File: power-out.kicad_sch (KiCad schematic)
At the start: 1 part, among them U2 TPS61022

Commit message: Configure power output
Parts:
- added C2: 10µF, symbol Device:C
- added C3, C4: 22µF, symbol Device:C
- added JP1: SolderJumper_2_Open, Jumper:SolderJumper-3_P1.3mm_Open_RoundedPad1.0x1.5mm_NumberLabels, symbol Jumper:SolderJumper_3_Open
- added L1: 1µH, symbol Device:L
- added R3: 402kΩ 1% 125mW, Resistor_SMD:R_0805_2012Metric_Pad1.20x1.40mm_HandSolder, symbol Device:R
- added R4: 88.7kΩ 1% 125mW, Resistor_SMD:R_0805_2012Metric_Pad1.20x1.40mm_HandSolder, symbol Device:R
- added R5, R6: 10kΩ 125mW, Resistor_SMD:R_0805_2012Metric_Pad1.20x1.40mm_HandSolder, symbol Device:R
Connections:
- net GND: now also C2.2, C3.2, C4.2, R4.2, R6.2
- net SUPERCAP: now also U2.5 (EN), C2.1, L1.1, R5.1
- net VOUT: now also C3.1, C4.1, R3.1
- net at U2.2 (SW): now also L1.2
- net at U2.4 (FB): now also R3.2, R4.1
- net at U2.6 (MODE): now also JP1.2 (C)
- new net: JP1.3 (B), R5.2
- new net: JP1.1 (A), R6.1
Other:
- moved on the sheet: U2

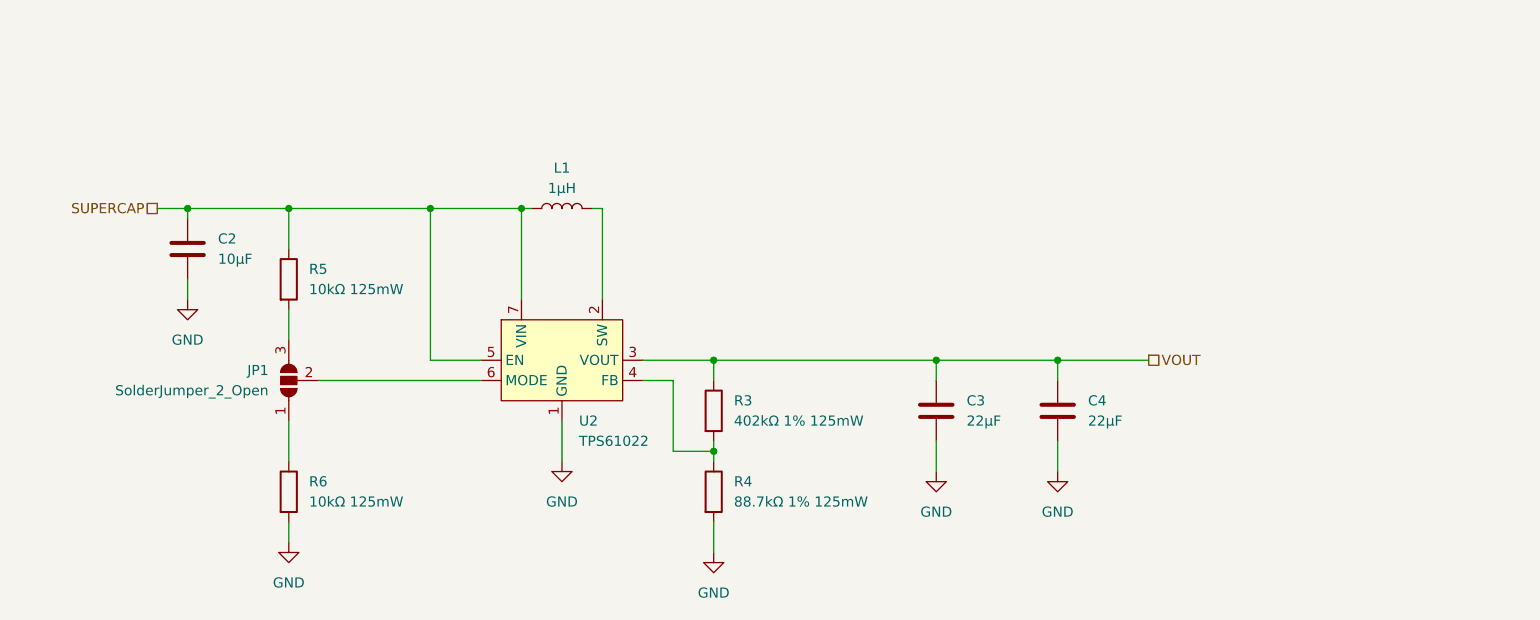
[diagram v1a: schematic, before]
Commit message: Add power output capacitors
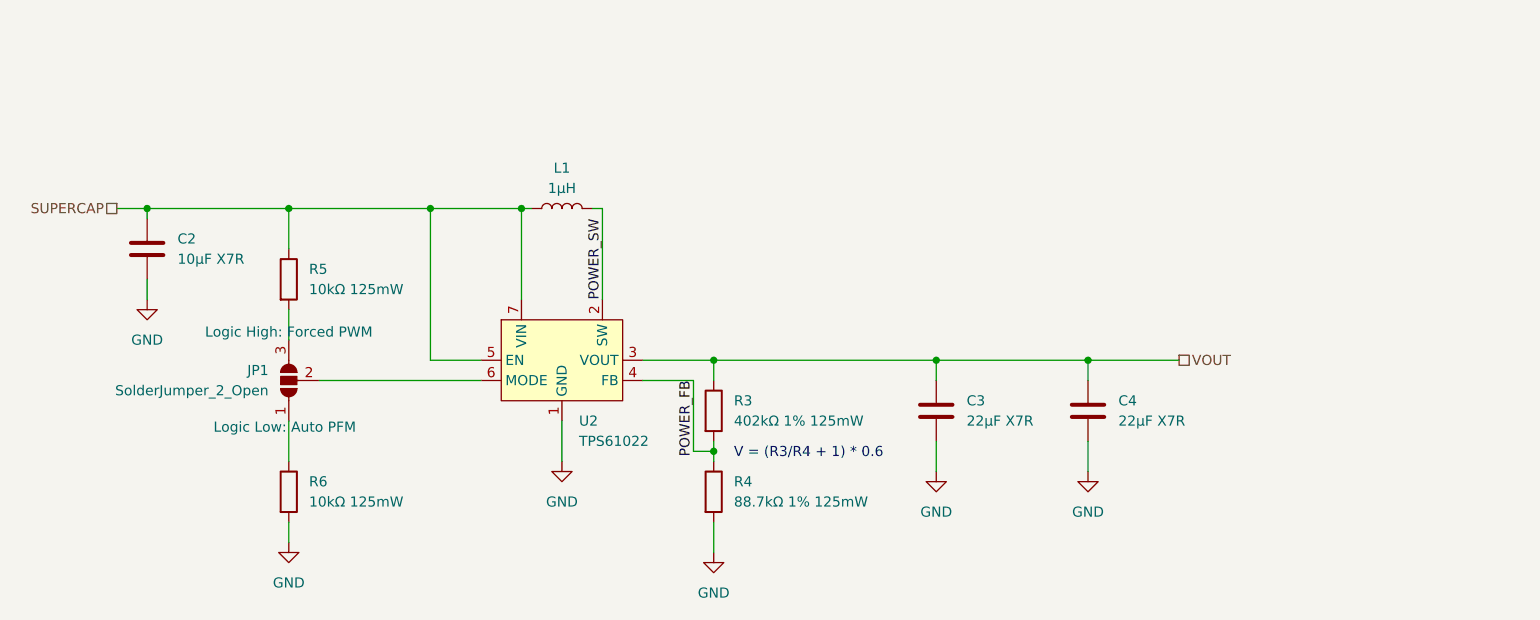
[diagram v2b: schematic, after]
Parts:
- C2: value 10µF -> 10µF X7R; footprint (none) -> Capacitor_SMD:C_0805_2012Metric_Pad1.18x1.45mm_HandSolder
- C3, C4: value 22µF -> 22µF X7R; footprint (none) -> Capacitor_SMD:C_0805_2012Metric_Pad1.18x1.45mm_HandSolder
- JP1: Logic High (none) -> Forced PWM; Logic Low (none) -> Auto PFM
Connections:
- net POWER_FB: now reaches R3.2, R4.1, U2.4 (FB)
- net POWER_SW: now reaches L1.2, U2.2 (SW)
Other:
- note added: "V = (R3/R4 + 1) * 0.6"
- moved on the sheet: C2, C4
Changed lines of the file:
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@@
 	(generator_version "9.0")
 	(paper "A4")
+	(text "V = (R3/R4 + 1) * 0.6"
+		(exclude_from_sim no)
+		(at 92.71 61.214 0)
+		(effects
+			(font
+				(size 1.27 1.27)
+			)
+			(justify left)
+		)
+	)
 	(junction
 		(at 90.17 49.53)
@@
 	)
 	(junction
-		(at 24.13 30.48)
+		(at 19.05 30.48)
 		(diameter 0)
 		(color 0 0 0 0)
@@
 	)
 	(junction
-		(at 133.35 49.53)
+		(at 137.16 49.53)
 		(diameter 0)
 		(color 0 0 0 0)
@@
 	(wire
 		(pts
+			(xy 118.11 49.53) (xy 137.16 49.53)
+		)
+		(stroke
+			(width 0)
+			(type default)
+		)
+	)
+	(wire
+		(pts
 			(xy 36.83 46.99) (xy 36.83 43.18)
 		)
@@
 	(wire
 		(pts
-			(xy 85.09 60.96) (xy 90.17 60.96)
-		)
-		(stroke
-			(width 0)
-			(type default)
-		)
-	)
-	(wire
-		(pts
-			(xy 133.35 49.53) (xy 144.78 49.53)
+			(xy 87.63 60.96) (xy 90.17 60.96)
+		)
+		(stroke
+			(width 0)
+			(type default)
+		)
+	)
+	(wire
+		(pts
+			(xy 137.16 49.53) (xy 148.59 49.53)
 		)
 		(stroke
@@
 	(wire
 		(pts
-			(xy 24.13 39.37) (xy 24.13 41.91)
+			(xy 19.05 39.37) (xy 19.05 41.91)
 		)
 		(stroke
@@
 	(wire
 		(pts
-			(xy 118.11 49.53) (xy 133.35 49.53)
-		)
-		(stroke
-			(width 0)
-			(type default)
-		)
-	)
-	(wire
-		(pts
-			(xy 24.13 31.75) (xy 24.13 30.48)
-		)
-		(stroke
-			(width 0)
-			(type default)
-		)
-	)
-	(wire
-		(pts
-			(xy 133.35 49.53) (xy 133.35 52.07)
-		)
-		(stroke
-			(width 0)
-			(type default)
-		)
-	)
-	(wire
-		(pts
-			(xy 85.09 52.07) (xy 85.09 60.96)
-		)
-		(stroke
-			(width 0)
-			(type default)
-		)
-	)
-	(wire
-		(pts
-			(xy 24.13 30.48) (xy 36.83 30.48)
+			(xy 19.05 31.75) (xy 19.05 30.48)
+		)
+		(stroke
+			(width 0)
+			(type default)
+		)
+	)
+	(wire
+		(pts
+			(xy 137.16 49.53) (xy 137.16 52.07)
+		)
+		(stroke
+			(width 0)
+			(type default)
+		)
+	)
+	(wire
+		(pts
+			(xy 87.63 52.07) (xy 87.63 60.96)
+		)
+		(stroke
+			(width 0)
+			(type default)
+		)
+	)
+	(wire
+		(pts
+			(xy 19.05 30.48) (xy 36.83 30.48)
 		)
 		(stroke
@@
 	(wire
 		(pts
-			(xy 133.35 59.69) (xy 133.35 63.5)
+			(xy 137.16 59.69) (xy 137.16 63.5)
 		)
 		(stroke
@@
 	(wire
 		(pts
-			(xy 81.28 52.07) (xy 85.09 52.07)
+			(xy 81.28 52.07) (xy 87.63 52.07)
 		)
 		(stroke
@@
 	(wire
 		(pts
-			(xy 20.32 30.48) (xy 24.13 30.48)
+			(xy 15.24 30.48) (xy 19.05 30.48)
 		)
 		(stroke
@@
 		)
 	)
-	(hierarchical_label "VOUT"
-		(shape passive)
-		(at 144.78 49.53 0)
+	(label "POWER_SW"
+		(at 76.2 31.75 270)
 		(effects
 			(font
 				(size 1.27 1.27)
 			)
-			(justify left)
-		)
-	)
-	(hierarchical_label "SUPERCAP"
-		(shape passive)
-		(at 20.32 30.48 180)
+			(justify right bottom)
+		)
+	)
+	(label "POWER_FB"
+		(at 87.63 52.07 270)
 		(effects
 			(font
 				(size 1.27 1.27)
 			)
+			(justify right bottom)
+		)
+	)
+	(hierarchical_label "VOUT"
+		(shape passive)
+		(at 148.59 49.53 0)
+		(effects
+			(font
+				(size 1.27 1.27)
+			)
+			(justify left)
+		)
+	)
+	(hierarchical_label "SUPERCAP"
+		(shape passive)
+		(at 15.24 30.48 180)
+		(effects
+			(font
+				(size 1.27 1.27)
+			)
 			(justify right)
 		)
@@
 	(symbol
 		(lib_id "Device:C")
-		(at 24.13 35.56 0)
+		(at 19.05 35.56 0)
 		(unit 1)
 		(exclude_from_sim no)
@@
 		(fields_autoplaced yes)
 		(property "Reference" "C2"
-			(at 27.94 34.2899 0)
-			(effects
-				(font
-					(size 1.27 1.27)
-				)
-				(justify left)
-			)
-		)
-		(property "Value" "10µF"
-			(at 27.94 36.8299 0)
-			(effects
-				(font
-					(size 1.27 1.27)
-				)
-				(justify left)
-			)
-		)
-		(property "Footprint" ""
-			(at 25.0952 39.37 0)
+			(at 22.86 34.2899 0)
+			(effects
+				(font
+					(size 1.27 1.27)
+				)
+				(justify left)
+			)
+		)
+		(property "Value" "10µF X7R"
+			(at 22.86 36.8299 0)
+			(effects
+				(font
+					(size 1.27 1.27)
+				)
+				(justify left)
+			)
+		)
+		(property "Footprint" "Capacitor_SMD:C_0805_2012Metric_Pad1.18x1.45mm_HandSolder"
+			(at 20.0152 39.37 0)
 			(effects
 				(font
@@
 		)
 		(property "Datasheet" "~"
-			(at 24.13 35.56 0)
+			(at 19.05 35.56 0)
 			(effects
 				(font
@@
 		)
 		(property "Description" "Unpolarized capacitor"
-			(at 24.13 35.56 0)
+			(at 19.05 35.56 0)
 			(effects
 				(font
@@
 	(symbol
 		(lib_id "Device:C")
-		(at 133.35 55.88 0)
+		(at 137.16 55.88 0)
 		(unit 1)
 		(exclude_from_sim no)
@@
 		(fields_autoplaced yes)
 		(property "Reference" "C4"
-			(at 137.16 54.6099 0)
-			(effects
-				(font
-					(size 1.27 1.27)
-				)
-				(justify left)
-			)
-		)
-		(property "Value" "22µF"
-			(at 137.16 57.1499 0)
-			(effects
-				(font
-					(size 1.27 1.27)
-				)
-				(justify left)
-			)
-		)
-		(property "Footprint" ""
-			(at 134.3152 59.69 0)
+			(at 140.97 54.6099 0)
+			(effects
+				(font
+					(size 1.27 1.27)
+				)
+				(justify left)
+			)
+		)
+		(property "Value" "22µF X7R"
+			(at 140.97 57.1499 0)
+			(effects
+				(font
+					(size 1.27 1.27)
+				)
+				(justify left)
+			)
+		)
+		(property "Footprint" "Capacitor_SMD:C_0805_2012Metric_Pad1.18x1.45mm_HandSolder"
+			(at 138.1252 59.69 0)
 			(effects
 				(font
@@
 		)
 		(property "Datasheet" "~"
-			(at 133.35 55.88 0)
+			(at 137.16 55.88 0)
 			(effects
 				(font
@@
 		)
 		(property "Description" "Unpolarized capacitor"
-			(at 133.35 55.88 0)
+			(at 137.16 55.88 0)
 			(effects
 				(font
@@
 	(symbol
 		(lib_id "power:GND")
-		(at 24.13 41.91 0)
+		(at 19.05 41.91 0)
 		(unit 1)
 		(exclude_from_sim no)
@@
 		(fields_autoplaced yes)
 		(property "Reference" "#PWR010"
-			(at 24.13 48.26 0)
+			(at 19.05 48.26 0)
 			(effects
 				(font
@@
 		)
 		(property "Value" "GND"
-			(at 24.13 46.99 0)
+			(at 19.05 46.99 0)
 			(effects
 				(font
@@
 		)
 		(property "Footprint" ""
-			(at 24.13 41.91 0)
+			(at 19.05 41.91 0)
 			(effects
 				(font
@@
 		)
 		(property "Datasheet" ""
-			(at 24.13 41.91 0)
+			(at 19.05 41.91 0)
 			(effects
 				(font
@@
 		)
 		(property "Description" "Power symbol creates a global label with name \"GND\" , ground"
-			(at 24.13 41.91 0)
+			(at 19.05 41.91 0)
 			(effects
 				(font
@@
 			)
 		)
-		(property "Value" "22µF"
+		(property "Value" "22µF X7R"
 			(at 121.92 57.1499 0)
 			(effects
@@
 			)
 		)
-		(property "Footprint" ""
+		(property "Footprint" "Capacitor_SMD:C_0805_2012Metric_Pad1.18x1.45mm_HandSolder"
 			(at 119.0752 59.69 0)
 			(effects
@@
 	(symbol
 		(lib_id "power:GND")
-		(at 133.35 63.5 0)
+		(at 137.16 63.5 0)
 		(unit 1)
 		(exclude_from_sim no)
@@
 		(fields_autoplaced yes)
 		(property "Reference" "#PWR011"
-			(at 133.35 69.85 0)
+			(at 137.16 69.85 0)
 			(effects
 				(font
@@
 		)
 		(property "Value" "GND"
-			(at 133.35 68.58 0)
+			(at 137.16 68.58 0)
 			(effects
 				(font
@@
 		)
 		(property "Footprint" ""
-			(at 133.35 63.5 0)
+			(at 137.16 63.5 0)
 			(effects
 				(font
@@
 		)
 		(property "Datasheet" ""
-			(at 133.35 63.5 0)
+			(at 137.16 63.5 0)
 			(effects
 				(font
@@
 		)
 		(property "Description" "Power symbol creates a global label with name \"GND\" , ground"
-			(at 133.35 63.5 0)
+			(at 137.16 63.5 0)
 			(effects
 				(font
@@
 		(on_board yes)
 		(dnp no)
-		(fields_autoplaced yes)
 		(property "Reference" "JP1"
 			(at 34.29 50.7999 90)
@@
 			)
 		)
+		(property "Logic High" "Forced PWM"
+			(at 36.83 45.974 90)
+			(show_name yes)
+			(effects
+				(font
+					(size 1.27 1.27)
+				)
+			)
+		)
+		(property "Logic Low" "Auto PFM"
+			(at 36.322 57.912 90)
+			(show_name yes)
+			(effects
+				(font
+					(size 1.27 1.27)
+				)
+			)
+		)

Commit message: Add inductor and finish power out layout
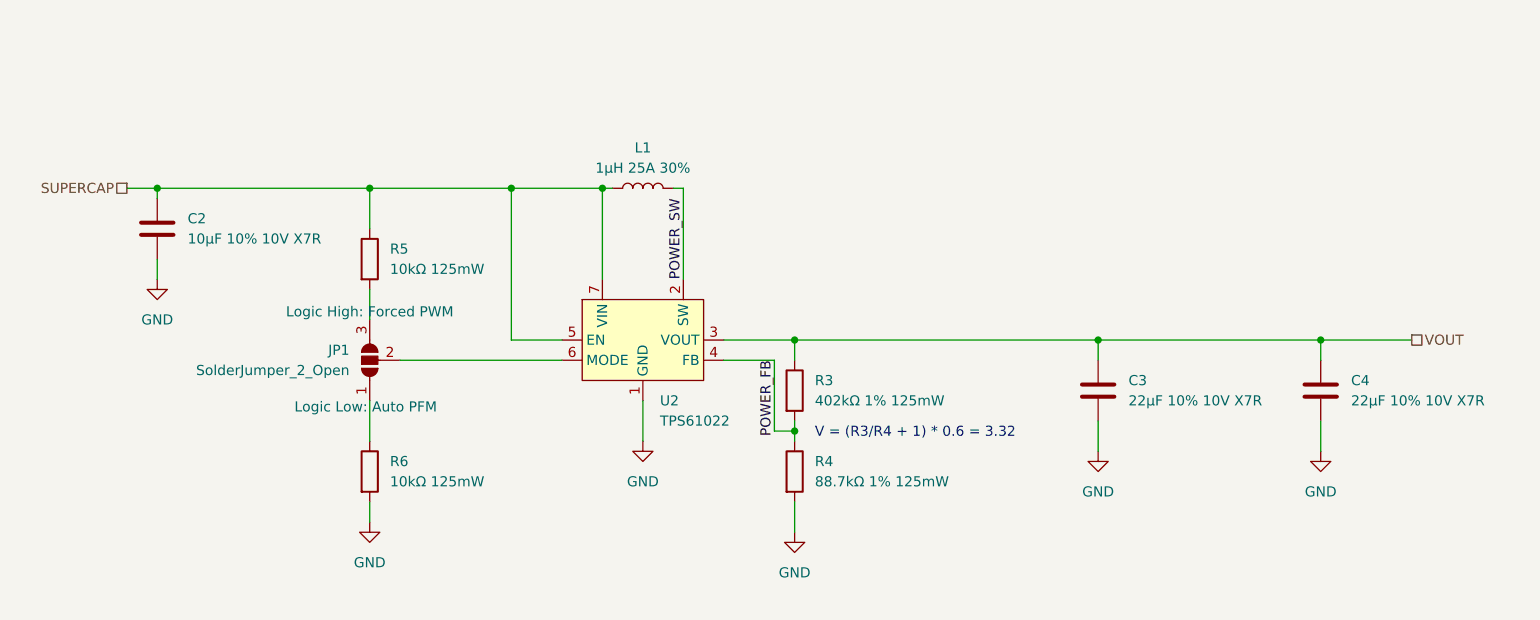
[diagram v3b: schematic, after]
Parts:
- C2: value 10µF X7R -> 10µF 10% 10V X7R
- C3, C4: value 22µF X7R -> 22µF 10% 10V X7R; footprint Capacitor_SMD:C_0805_2012Metric_Pad1.18x1.45mm_HandSolder -> Capacitor_SMD:C_1206_3216Metric_Pad1.33x1.80mm_HandSolder
- L1: value 1µH -> 1µH 25A 30%; footprint (none) -> Inductor_SMD:L_Bourns_SRP1245A
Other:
- note added: "V = (R3/R4 + 1) * 0.6 = 3.32"
- note removed: "V = (R3/R4 + 1) * 0.6"
- moved on the sheet: C2, C3, C4, JP1, L1, R3, R4, R5, R6, U2

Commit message: Prefix all of the references so that the numbering is manageable across multiple circuits
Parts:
- renumbered C2 to P.C1, C3 to P.C2, C4 to P.C3, JP1 to P.JP1, L1 to P.L1, R3 to P.R1, R4 to P.R2, R5 to P.R3, R6 to P.R4, U2 to P.U1
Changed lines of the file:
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@@
 		(dnp no)
 		(fields_autoplaced yes)
-		(property "Reference" "C2"
+		(property "Reference" "P.C1"
 			(at 24.13 31.7499 0)
 			(effects
@@
 			(project ""
 				(path "/01e6e533-9ed1-4dde-bac5-1959ff8991e5/08e0040f-7161-45a0-9f3d-7aa124b5aeed"
-					(reference "C2")
+					(reference "P.C1")
 					(unit 1)
 				)
@@
 		(dnp no)
 		(fields_autoplaced yes)
-		(property "Reference" "R4"
+		(property "Reference" "P.R2"
 			(at 102.87 62.2299 0)
 			(effects
@@
 			(project ""
 				(path "/01e6e533-9ed1-4dde-bac5-1959ff8991e5/08e0040f-7161-45a0-9f3d-7aa124b5aeed"
-					(reference "R4")
+					(reference "P.R2")
 					(unit 1)
 				)
@@
 		(dnp no)
 		(fields_autoplaced yes)
-		(property "Reference" "L1"
+		(property "Reference" "P.L1"
 			(at 81.28 22.86 90)
 			(effects
@@
 			(project ""
 				(path "/01e6e533-9ed1-4dde-bac5-1959ff8991e5/08e0040f-7161-45a0-9f3d-7aa124b5aeed"
-					(reference "L1")
+					(reference "P.L1")
 					(unit 1)
 				)
@@
 		(dnp no)
 		(fields_autoplaced yes)
-		(property "Reference" "C4"
+		(property "Reference" "P.C3"
 			(at 170.18 52.0699 0)
 			(effects
@@
 			(project "wireless-3v3-supercap"
 				(path "/01e6e533-9ed1-4dde-bac5-1959ff8991e5/08e0040f-7161-45a0-9f3d-7aa124b5aeed"
-					(reference "C4")
+					(reference "P.C3")
 					(unit 1)
 				)
@@
 		(dnp no)
 		(fields_autoplaced yes)
-		(property "Reference" "C3"
+		(property "Reference" "P.C2"
 			(at 142.24 52.0699 0)
 			(effects
@@
 			(project ""
 				(path "/01e6e533-9ed1-4dde-bac5-1959ff8991e5/08e0040f-7161-45a0-9f3d-7aa124b5aeed"
-					(reference "C3")
+					(reference "P.C2")
 					(unit 1)
 				)
@@
 		(dnp no)
 		(fields_autoplaced yes)
-		(property "Reference" "R5"
+		(property "Reference" "P.R3"
 			(at 49.53 35.5599 0)
 			(effects
@@
 			(project ""
 				(path "/01e6e533-9ed1-4dde-bac5-1959ff8991e5/08e0040f-7161-45a0-9f3d-7aa124b5aeed"
-					(reference "R5")
+					(reference "P.R3")
 					(unit 1)
 				)
@@
 		(dnp no)
 		(fields_autoplaced yes)
-		(property "Reference" "R3"
+		(property "Reference" "P.R1"
 			(at 102.87 52.0699 0)
 			(effects
@@
 			(project ""
 				(path "/01e6e533-9ed1-4dde-bac5-1959ff8991e5/08e0040f-7161-45a0-9f3d-7aa124b5aeed"
-					(reference "R3")
+					(reference "P.R1")
 					(unit 1)
 				)
@@
 		(dnp no)
 		(fields_autoplaced yes)
-		(property "Reference" "U2"
+		(property "Reference" "P.U1"
 			(at 83.4233 54.61 0)
 			(effects
@@
 			(project ""
 				(path "/01e6e533-9ed1-4dde-bac5-1959ff8991e5/08e0040f-7161-45a0-9f3d-7aa124b5aeed"
-					(reference "U2")
+					(reference "P.U1")
 					(unit 1)
 				)
@@
 		(on_board yes)
 		(dnp no)
-		(property "Reference" "JP1"
+		(property "Reference" "P.JP1"
 			(at 44.45 48.2599 90)
 			(effects
@@
 			(project ""
 				(path "/01e6e533-9ed1-4dde-bac5-1959ff8991e5/08e0040f-7161-45a0-9f3d-7aa124b5aeed"
-					(reference "JP1")
+					(reference "P.JP1")
 					(unit 1)
 				)
@@
 		(dnp no)
 		(fields_autoplaced yes)
-		(property "Reference" "R6"
+		(property "Reference" "P.R4"
 			(at 49.53 62.2299 0)
 			(effects
@@
 			(project "wireless-3v3-supercap"
 				(path "/01e6e533-9ed1-4dde-bac5-1959ff8991e5/08e0040f-7161-45a0-9f3d-7aa124b5aeed"
-					(reference "R6")
-					(unit 1)
-				)
+					(reference "P.R4")
+					(unit 1)
+				)

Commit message: Add voltage divider circuit for ADC
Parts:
- P.R3, P.R4: value 10kΩ 125mW -> 10kΩ 1% 125mW
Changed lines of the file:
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@@
 			)
 		)
-		(property "Value" "10kΩ 125mW"
+		(property "Value" "10kΩ 1% 125mW"
 			(at 49.53 38.0999 0)
 			(effects
@@
 			)
 		)
-		(property "Value" "10kΩ 125mW"
+		(property "Value" "10kΩ 1% 125mW"
 			(at 49.53 64.7699 0)
 			(effects

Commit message: Add incomplete charge circuit
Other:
- moved on the sheet: P.C1, P.C2, P.C3, P.JP1, P.L1, P.R1, P.R2, P.R3, P.R4, P.U1

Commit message: Finish charge circuit
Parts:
- P.L1: value 1µH 25A 30% -> 1µH 25A 20%
- P.R1: value 402kΩ 1% 125mW -> 402kΩ 0.1% 125mW
- P.R2: value 88.7kΩ 1% 125mW -> 88.7kΩ 0.1% 125mW
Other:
- note added: "V = 0.6 * (1 + R3/R4) = 3.319"
- note removed: "V = (R3/R4 + 1) * 0.6 = 3.32"
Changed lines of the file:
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@@
 	(generator_version "9.0")
 	(paper "User" 195 70)
-	(text "V = (R3/R4 + 1) * 0.6 = 3.32"
+	(text "V = 0.6 * (1 + R3/R4) = 3.319"
 		(exclude_from_sim no)
 		(at 102.87 43.434 0)
@@
 			)
 		)
-		(property "Value" "88.7kΩ 1% 125mW"
+		(property "Value" "88.7kΩ 0.1% 125mW"
 			(at 102.87 49.5299 0)
 			(effects
@@
 			)
 		)
-		(property "Value" "1µH 25A 30%"
+		(property "Value" "1µH 25A 20%"
 			(at 81.28 10.16 90)
 			(effects
@@
 			)
 		)
-		(property "Value" "402kΩ 1% 125mW"
+		(property "Value" "402kΩ 0.1% 125mW"
 			(at 102.87 39.3699 0)
 			(effects
